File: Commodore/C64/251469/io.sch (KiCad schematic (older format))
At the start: 24 parts, among them CN8 Control Port 2, CN9 Control Port 1, U1 6526, U2 6526, U27 74LS08, U28 4066, U8 7406

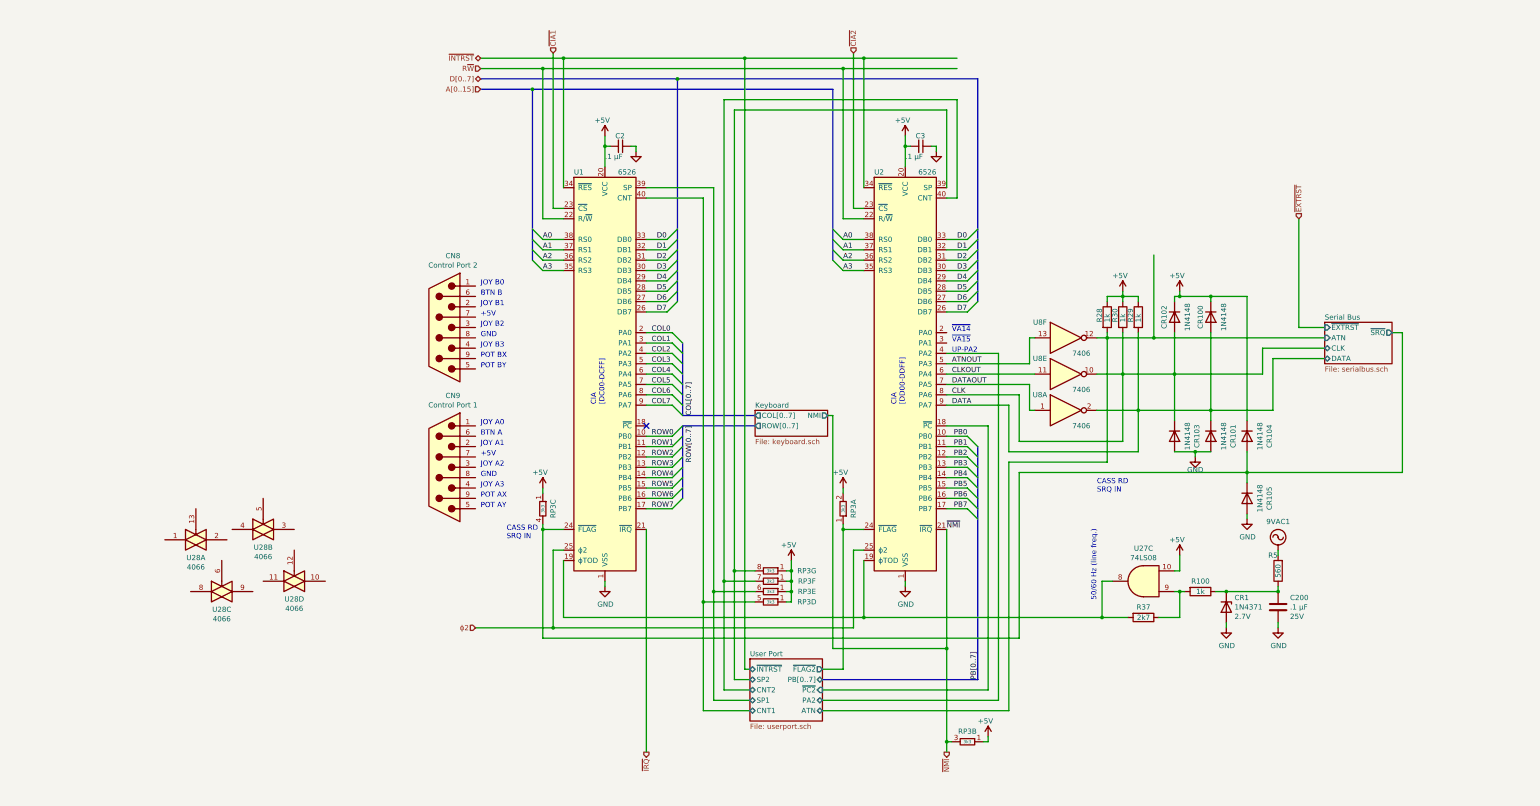
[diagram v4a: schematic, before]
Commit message: Tightened up diode clamp part of IO section
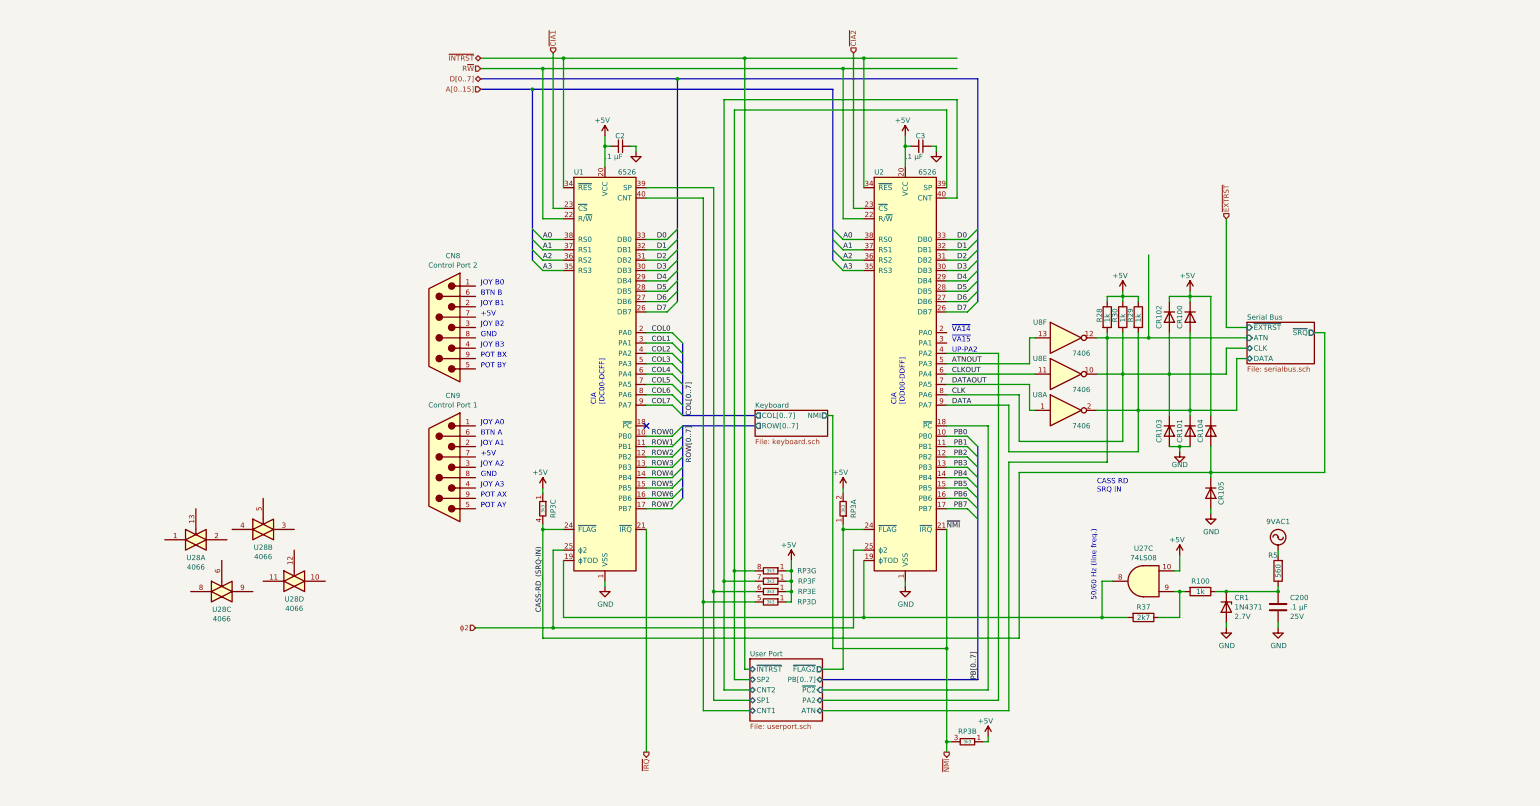
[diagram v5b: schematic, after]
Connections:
- net Serial Bus/~SRQ renamed CASS-RD_(SRQ-IN)
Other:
- moved on the sheet: CR100, CR101, CR102, CR103, CR104, CR105
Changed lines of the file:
@@
 ~NMI
-$Comp
-L Device:D CR101
-U 1 1 5D6E1332
-P 8150 4450
-F 0 "CR101" H 8150 4666 50  0000 C CNN
-F 1 "1N4148" H 8150 4575 50  0000 C CNN
-F 2 "" H 8150 4450 50  0001 C CNN
-F 3 "~" H 8150 4450 50  0001 C CNN
-	1    8150 4450
-	0    1    1    0
-$EndComp
-$Comp
-L Device:D CR103
-U 1 1 5D6E318C
-P 7800 4450
-F 0 "CR103" H 7800 4666 50  0000 C CNN
-F 1 "1N4148" H 7800 4575 50  0000 C CNN
-F 2 "" H 7800 4450 50  0001 C CNN
-F 3 "~" H 7800 4450 50  0001 C CNN
-	1    7800 4450
-	0    1    1    0
-$EndComp
-$Comp
-L Device:D CR104
-U 1 1 5D6E99E9
-P 8500 4450
-F 0 "CR104" H 8500 4666 50  0000 C CNN
-F 1 "1N4148" H 8500 4575 50  0000 C CNN
-F 2 "" H 8500 4450 50  0001 C CNN
-F 3 "~" H 8500 4450 50  0001 C CNN
-	1    8500 4450
-	0    1    1    0
-$EndComp
 $Comp
 L Device:D CR105
 U 1 1 5D6E99EF
-P 8500 5050
-F 0 "CR105" H 8500 5266 50  0000 C CNN
-F 1 "1N4148" H 8500 5175 50  0000 C CNN
-F 2 "" H 8500 5050 50  0001 C CNN
-F 3 "~" H 8500 5050 50  0001 C CNN
-	1    8500 5050
-	0    1    1    0
-$EndComp
-Text Notes 1350 5450 0    50   ~ 0
-CASS RD\nSRQ IN
+P 8150 5000
+F 0 "CR105" H 8150 5100 50  0000 C CNN
+F 1 "1N4148" H 8150 5125 50  0001 C CNN
+F 2 "" H 8150 5000 50  0001 C CNN
+F 3 "~" H 8150 5000 50  0001 C CNN
+	1    8150 5000
+	0    1    1    0
+$EndComp
 Text Notes 5650 3450 0    50   ~ 0
 ~VA14
@@
 Connection ~ 7150 3500
 $Comp
-L Device:R R28
-U 1 1 5DA82DAB
-P 7150 3300
-F 0 "R28" V 7075 3250 50  0000 L CNN
-F 1 "1k" V 7150 3250 50  0000 L CNN
-F 2 "" V 7080 3300 50  0001 C CNN
-F 3 "~" H 7150 3300 50  0001 C CNN
-	1    7150 3300
-	1    0    0    -1
-$EndComp
-$Comp
 L Device:R R30
 U 1 1 5DA836EF
@@
 Connection ~ 7300 3850
 Wire Wire Line
-	7150 3500 7600 3500
+	7150 3500 7550 3500
 Wire Wire Line
 	7050 4200 7450 4200
@@
 	7450 4600 7450 4200
 Wire Wire Line
-	7600 3500 7600 2700
-Wire Wire Line
-	7450 4200 8150 4200
-Wire Wire Line
-	8150 4200 8150 4300
-Connection ~ 7800 3850
-Wire Wire Line
-	7800 3850 7800 4300
-Wire Wire Line
-	7300 3850 7800 3850
-Connection ~ 8150 4200
-Wire Wire Line
-	7800 3850 7800 3450
+	7550 3500 7550 2700
+Wire Wire Line
+	7450 4200 7950 4200
+Connection ~ 7750 3850
+Wire Wire Line
+	7750 3850 7750 4250
+Wire Wire Line
+	7300 3850 7750 3850
+Connection ~ 7950 4200
+Wire Wire Line
+	7750 3850 7750 3450
 $Comp
 L Device:D CR102
 U 1 1 5D6E3186
-P 7800 3300
-F 0 "CR102" H 7800 3200 50  0000 C CNN
-F 1 "1N4148" H 7800 3425 50  0000 C CNN
-F 2 "" H 7800 3300 50  0001 C CNN
-F 3 "~" H 7800 3300 50  0001 C CNN
-	1    7800 3300
-	0    1    1    0
-$EndComp
-Wire Wire Line
-	7800 3150 7800 3100
-Wire Wire Line
-	7850 3100 8150 3100
-Connection ~ 7850 3100
-Wire Wire Line
-	7850 3050 7850 3100
+P 7750 3300
+F 0 "CR102" H 7750 3200 50  0000 C CNN
+F 1 "1N4148" H 7750 3425 50  0001 C CNN
+F 2 "" H 7750 3300 50  0001 C CNN
+F 3 "~" H 7750 3300 50  0001 C CNN
+	1    7750 3300
+	0    1    1    0
+$EndComp
+Wire Wire Line
+	7750 3150 7750 3100
+Wire Wire Line
+	7750 3100 7950 3100
+Wire Wire Line
+	7950 3050 7950 3100
 $Comp
 L power:+5V #PWR?
 U 1 1 5DD390BE
-P 7850 3050
+P 7950 3050
 AR Path="/5DD390BE" Ref="#PWR?"  Part="1"
 AR Path="/5D28EBAC/5DD390BE" Ref="#PWR?"  Part="1"
@@
 AR Path="/5D943305/5DD390BE" Ref="#PWR?"  Part="1"
 AR Path="/5D943305/5D47A471/5DD390BE" Ref="#PWR?"  Part="1"
-F 0 "#PWR?" H 7850 2900 50  0001 C CNN
-F 1 "+5V" H 7750 3200 50  0000 L CNN
-F 2 "" H 7850 3050 50  0001 C CNN
-F 3 "" H 7850 3050 50  0001 C CNN
-	1    7850 3050
-	1    0    0    -1
-$EndComp
-Wire Wire Line
-	8150 3100 8150 3150
-Wire Wire Line
-	7800 3100 7850 3100
-Wire Wire Line
-	8150 4200 8150 3450
+F 0 "#PWR?" H 7950 2900 50  0001 C CNN
+F 1 "+5V" H 7850 3200 50  0000 L CNN
+F 2 "" H 7950 3050 50  0001 C CNN
+F 3 "" H 7950 3050 50  0001 C CNN
+	1    7950 3050
+	1    0    0    -1
+$EndComp
+Wire Wire Line
+	7950 3100 7950 3150
+Wire Wire Line
+	7950 4200 7950 3450
 $Comp
 L Device:D CR100
 U 1 1 5D6E038A
-P 8150 3300
-F 0 "CR100" H 8150 3200 50  0000 C CNN
-F 1 "1N4148" H 8150 3425 50  0000 C CNN
-F 2 "" H 8150 3300 50  0001 C CNN
-F 3 "~" H 8150 3300 50  0001 C CNN
-	1    8150 3300
-	0    1    1    0
-$EndComp
-Connection ~ 7600 3500
+P 7950 3300
+F 0 "CR100" H 7950 3200 50  0000 C CNN
+F 1 "1N4148" H 7950 3425 50  0001 C CNN
+F 2 "" H 7950 3300 50  0001 C CNN
+F 3 "~" H 7950 3300 50  0001 C CNN
+	1    7950 3300
+	0    1    1    0
+$EndComp
+Connection ~ 7550 3500
 $Sheet
-S 9250 3350 650  400
+S 8500 3350 650  400
 U 5DDE0343
 F0 "Serial Bus" 50
 F1 "serialbus.sch" 50
-F2 "~EXTRST" I L 9250 3400 50
-F3 "ATN" I L 9250 3500 50
-F4 "CLK" B L 9250 3600 50
-F5 "DATA" B L 9250 3700 50
-F6 "~SRQ" O R 9900 3450 50
+F2 "~EXTRST" I L 8500 3400 50
+F3 "ATN" I L 8500 3500 50
+F4 "CLK" B L 8500 3600 50
+F5 "DATA" B L 8500 3700 50
+F6 "~SRQ" O R 9150 3450 50
 $EndSheet
 Connection ~ 4600 5350
@@
 Connection ~ 1700 5350
 Wire Wire Line
-	6300 4800 8500 4800
-Wire Wire Line
-	8150 4200 8750 4200
-Wire Wire Line
-	7800 3850 8650 3850
-Wire Wire Line
-	8500 4300 8500 3100
-Wire Wire Line
-	8500 3100 8150 3100
-Connection ~ 8150 3100
-Wire Wire Line
-	8500 4800 8500 4600
-Connection ~ 8500 4800
-Wire Wire Line
-	8500 4800 8500 4900
-Wire Wire Line
-	8150 4600 8000 4600
-$Comp
-L power:GND #PWR?
-U 1 1 5DFF36EE
-P 8000 4650
-F 0 "#PWR?" H 8000 4400 50  0001 C CNN
-F 1 "GND" H 8000 4525 50  0000 C CNN
-F 2 "" H 8000 4650 50  0001 C CNN
-F 3 "" H 8000 4650 50  0001 C CNN
-	1    8000 4650
-	1    0    0    -1
-$EndComp
-Wire Wire Line
-	8000 4650 8000 4600
-Connection ~ 8000 4600
-Wire Wire Line
-	8000 4600 7800 4600
+	6300 4800 8150 4800
+Wire Wire Line
+	7950 4200 8400 4200
+Wire Wire Line
+	7750 3850 8300 3850
+Wire Wire Line
+	8150 3100 7950 3100
+Connection ~ 7950 3100
+Connection ~ 8150 4800
+Wire Wire Line
+	8150 4800 8150 4850
 $Comp
 L power:GND #PWR?
 U 1 1 5E000C0D
-P 8500 5250
-F 0 "#PWR?" H 8500 5000 50  0001 C CNN
-F 1 "GND" H 8505 5077 50  0000 C CNN
-F 2 "" H 8500 5250 50  0001 C CNN
-F 3 "" H 8500 5250 50  0001 C CNN
-	1    8500 5250
-	1    0    0    -1
-$EndComp
-Wire Wire Line
-	8500 5250 8500 5200
-Wire Wire Line
-	10000 4800 10000 3450
-Wire Wire Line
-	8500 4800 10000 4800
-Wire Wire Line
-	7600 3500 9250 3500
-Wire Wire Line
-	9250 3400 9000 3400
-Wire Wire Line
-	9000 3400 9000 2350
-Text HLabel 9000 2350 1    50   Input ~ 0
+P 8150 5200
+F 0 "#PWR?" H 8150 4950 50  0001 C CNN
+F 1 "GND" H 8155 5027 50  0000 C CNN
+F 2 "" H 8150 5200 50  0001 C CNN
+F 3 "" H 8150 5200 50  0001 C CNN
+	1    8150 5200
+	1    0    0    -1
+$EndComp
+Wire Wire Line
+	8150 5200 8150 5150
+Wire Wire Line
+	9250 4800 9250 3450
+Wire Wire Line
+	8150 4800 9250 4800
+Wire Wire Line
+	7550 3500 8500 3500
+Wire Wire Line
+	8500 3400 8300 3400
+Wire Wire Line
+	8300 3400 8300 2350
+Text HLabel 8300 2350 1    50   Input ~ 0
 ~EXTRST
 Wire Wire Line
-	8650 3600 9250 3600
-Wire Wire Line
-	8650 3600 8650 3850
-Wire Wire Line
-	8750 3700 9250 3700
-Wire Wire Line
-	8750 3700 8750 4200
-Wire Wire Line
-	10000 3450 9900 3450
+	8300 3600 8500 3600
+Wire Wire Line
+	8300 3600 8300 3850
+Wire Wire Line
+	8400 3700 8500 3700
+Wire Wire Line
+	8400 3700 8400 4200
+Wire Wire Line
+	9250 3450 9150 3450
 Wire Wire Line
 	4600 4950 4600 5000
@@
 F 3 "http://www.vishay.com/docs/31509/csc.pdf" H 3900 6050 50  0001 C CNN
 	4    3900 6050
+	0    1    1    0
+$EndComp
+Text Label 5600 5350 0    50   ~ 0
+~NMI
+Text Label 5650 3750 0    50   ~ 0
+ATNOUT
+Text Label 5650 3850 0    50   ~ 0
+CLKOUT
+Text Label 5650 3950 0    50   ~ 0
+DATAOUT
+Text Label 5650 4050 0    50   ~ 0
+CLK
+Text Label 5650 4150 0    50   ~ 0
+DATA
+$Comp
+L Device:R R28
+U 1 1 5DA82DAB
+P 7150 3300
+F 0 "R28" V 7075 3250 50  0000 L CNN
+F 1 "1k" V 7150 3250 50  0000 L CNN
+F 2 "" V 7080 3300 50  0001 C CNN
+F 3 "~" H 7150 3300 50  0001 C CNN
+	1    7150 3300
+	1    0    0    -1
+$EndComp
+$Comp
+L Device:D CR103
+U 1 1 5D6E318C
+P 7750 4400
+F 0 "CR103" H 7750 4300 50  0000 C CNN
+F 1 "1N4148" H 7750 4500 50  0001 C CNN
+F 2 "" H 7750 4400 50  0001 C CNN
+F 3 "~" H 7750 4400 50  0001 C CNN
+	1    7750 4400
+	0    1    1    0
+$EndComp
+Wire Wire Line
+	7750 4550 7850 4550
+$Comp
+L power:GND #PWR?
+U 1 1 5DFF36EE
+P 7850 4600
+F 0 "#PWR?" H 7850 4350 50  0001 C CNN
+F 1 "GND" H 7850 4475 50  0000 C CNN
+F 2 "" H 7850 4600 50  0001 C CNN
+F 3 "" H 7850 4600 50  0001 C CNN
+	1    7850 4600
+	1    0    0    -1
+$EndComp
+Wire Wire Line
+	7850 4600 7850 4550
+Connection ~ 7850 4550
+Wire Wire Line
+	7850 4550 7950 4550
+Wire Wire Line
+	7950 4200 7950 4250
+$Comp
+L Device:D CR101
+U 1 1 5D6E1332
+P 7950 4400
+F 0 "CR101" H 7950 4300 50  0000 C CNN
+F 1 "1N4148" H 7950 4500 50  0001 C CNN
+F 2 "" H 7950 4400 50  0001 C CNN
+F 3 "~" H 7950 4400 50  0001 C CNN
+	1    7950 4400
+	0    1    1    0
+$EndComp
+Wire Wire Line
+	8150 4800 8150 4550
+Wire Wire Line
+	8150 4250 8150 3100
+$Comp
+L Device:D CR104
+U 1 1 5D6E99E9
+P 8150 4400
+F 0 "CR104" H 8150 4300 50  0000 C CNN
+F 1 "1N4148" H 8150 4500 50  0001 C CNN
+F 2 "" H 8150 4400 50  0001 C CNN
+F 3 "~" H 8150 4400 50  0001 C CNN
+	1    8150 4400
 	0    1    1    0
 $EndComp
@@
 Wire Bus Line
 	3000 1000 3000 3150
-Text Label 5600 5350 0    50   ~ 0
-~NMI
-Text Label 5650 3750 0    50   ~ 0
-ATNOUT
-Text Label 5650 3850 0    50   ~ 0
-CLKOUT
-Text Label 5650 3950 0    50   ~ 0
-DATAOUT
-Text Label 5650 4050 0    50   ~ 0
-CLK
-Text Label 5650 4150 0    50   ~ 0
-DATA
+Text Label 1700 6150 1    50   ~ 0
+CASS-RD_(SRQ-IN)
 $EndSCHEMATC

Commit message: WIP
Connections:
- net TOD: now reaches R37.2, U1.19 (ϕTOD), U2.19 (ϕTOD), U27.8
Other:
- note removed: "CASS RD\nSRQ IN"
- moved on the sheet: C200, CR1, R100, R37, R5, U27C
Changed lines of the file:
@@
 L Device:R R37
 U 1 1 5D3AB7B9
-P 7500 6200
-F 0 "R37" V 7400 6200 50  0000 C CNN
-F 1 "2k7" V 7500 6200 50  0000 C CNN
-F 2 "" V 7430 6200 50  0001 C CNN
-F 3 "~" H 7500 6200 50  0001 C CNN
-	1    7500 6200
+P 9550 6200
+F 0 "R37" V 9450 6200 50  0000 C CNN
+F 1 "2k7" V 9550 6200 50  0000 C CNN
+F 2 "" V 9480 6200 50  0001 C CNN
+F 3 "~" H 9550 6200 50  0001 C CNN
+	1    9550 6200
 	0    1    1    0
 $EndComp
@@
 L Device:R R100
 U 1 1 5D3AC837
-P 8050 5950
-F 0 "R100" V 7950 5950 50  0000 C CNN
-F 1 "1k" V 8050 5950 50  0000 C CNN
-F 2 "" V 7980 5950 50  0001 C CNN
-F 3 "~" H 8050 5950 50  0001 C CNN
-	1    8050 5950
+P 10100 5950
+F 0 "R100" V 10000 5950 50  0000 C CNN
+F 1 "1k" V 10100 5950 50  0000 C CNN
+F 2 "" V 10030 5950 50  0001 C CNN
+F 3 "~" H 10100 5950 50  0001 C CNN
+	1    10100 5950
 	0    1    1    0
 $EndComp
@@
 L Device:D_Zener CR1
 U 1 1 5D3AF3BF
-P 8300 6100
-F 0 "CR1" V 8209 6179 50  0000 L CNN
-F 1 "1N4371" V 8300 6179 50  0000 L CNN
-F 2 "" H 8300 6100 50  0001 C CNN
-F 3 "~" H 8300 6100 50  0001 C CNN
-F 4 "2.7V" V 8391 6179 50  0000 L CNN "Zener Voltage"
-	1    8300 6100
+P 10350 6100
+F 0 "CR1" V 10259 6179 50  0000 L CNN
+F 1 "1N4371" V 10350 6179 50  0000 L CNN
+F 2 "" H 10350 6100 50  0001 C CNN
+F 3 "~" H 10350 6100 50  0001 C CNN
+F 4 "2.7V" V 10441 6179 50  0000 L CNN "Zener Voltage"
+	1    10350 6100
 	0    1    1    0
 $EndComp
@@
 L Device:C C200
 U 1 1 5D3B049D
-P 8800 6100
-F 0 "C200" H 8915 6191 50  0000 L CNN
-F 1 ".1 μF" H 8915 6100 50  0000 L CNN
-F 2 "" H 8838 5950 50  0001 C CNN
-F 3 "~" H 8800 6100 50  0001 C CNN
-F 4 "25V" H 8915 6009 50  0000 L CNN "Voltage Rating"
-	1    8800 6100
+P 10850 6100
+F 0 "C200" H 10965 6191 50  0000 L CNN
+F 1 ".1 μF" H 10965 6100 50  0000 L CNN
+F 2 "" H 10888 5950 50  0001 C CNN
+F 3 "~" H 10850 6100 50  0001 C CNN
+F 4 "25V" H 10965 6009 50  0000 L CNN "Voltage Rating"
+	1    10850 6100
 	1    0    0    -1
 $EndComp
@@
 L power_more:9VAC1 #PWR?
 U 1 1 5D3B15DC
-P 8800 5550
-F 0 "#PWR?" H 8800 5450 50  0001 C CNN
-F 1 "9VAC1" H 8800 5825 50  0000 C CNN
-F 2 "" H 8800 5550 50  0001 C CNN
-F 3 "" H 8800 5550 50  0001 C CNN
-	1    8800 5550
-	1    0    0    -1
-$EndComp
-Wire Wire Line
-	8800 5550 8800 5600
-Wire Wire Line
-	8800 5900 8800 5950
+P 10850 5550
+F 0 "#PWR?" H 10850 5450 50  0001 C CNN
+F 1 "9VAC1" H 10850 5825 50  0000 C CNN
+F 2 "" H 10850 5550 50  0001 C CNN
+F 3 "" H 10850 5550 50  0001 C CNN
+	1    10850 5550
+	1    0    0    -1
+$EndComp
+Wire Wire Line
+	10850 5550 10850 5600
+Wire Wire Line
+	10850 5900 10850 5950
 $Comp
 L power:GND #PWR?
 U 1 1 5D3B771F
-P 8800 6300
-F 0 "#PWR?" H 8800 6050 50  0001 C CNN
-F 1 "GND" H 8805 6127 50  0000 C CNN
-F 2 "" H 8800 6300 50  0001 C CNN
-F 3 "" H 8800 6300 50  0001 C CNN
-	1    8800 6300
-	1    0    0    -1
-$EndComp
-Wire Wire Line
-	8800 6250 8800 6300
+P 10850 6300
+F 0 "#PWR?" H 10850 6050 50  0001 C CNN
+F 1 "GND" H 10855 6127 50  0000 C CNN
+F 2 "" H 10850 6300 50  0001 C CNN
+F 3 "" H 10850 6300 50  0001 C CNN
+	1    10850 6300
+	1    0    0    -1
+$EndComp
+Wire Wire Line
+	10850 6250 10850 6300
 $Comp
 L power:GND #PWR?
 U 1 1 5D3B8BE9
-P 8300 6300
-F 0 "#PWR?" H 8300 6050 50  0001 C CNN
-F 1 "GND" H 8305 6127 50  0000 C CNN
-F 2 "" H 8300 6300 50  0001 C CNN
-F 3 "" H 8300 6300 50  0001 C CNN
-	1    8300 6300
-	1    0    0    -1
-$EndComp
-Wire Wire Line
-	8300 6250 8300 6300
-Wire Wire Line
-	8300 5950 8800 5950
-Connection ~ 8800 5950
+P 10350 6300
+F 0 "#PWR?" H 10350 6050 50  0001 C CNN
+F 1 "GND" H 10355 6127 50  0000 C CNN
+F 2 "" H 10350 6300 50  0001 C CNN
+F 3 "" H 10350 6300 50  0001 C CNN
+	1    10350 6300
+	1    0    0    -1
+$EndComp
+Wire Wire Line
+	10350 6250 10350 6300
+Wire Wire Line
+	10350 5950 10850 5950
+Connection ~ 10850 5950
 $Comp
 L Device:R R5
 U 1 1 5D3AD8AF
-P 8800 5750
-F 0 "R5" H 8850 5600 50  0000 C CNN
-F 1 "560" V 8800 5750 50  0000 C CNN
-F 2 "" V 8730 5750 50  0001 C CNN
-F 3 "~" H 8800 5750 50  0001 C CNN
-	1    8800 5750
+P 10850 5750
+F 0 "R5" H 10900 5600 50  0000 C CNN
+F 1 "560" V 10850 5750 50  0000 C CNN
+F 2 "" V 10780 5750 50  0001 C CNN
+F 3 "~" H 10850 5750 50  0001 C CNN
+	1    10850 5750
 	-1   0    0    1
 $EndComp
@@
 L power:+5V #PWR?
 U 1 1 5D3C4989
-P 7850 5600
+P 9900 5600
 AR Path="/5D3C4989" Ref="#PWR?"  Part="1"
 AR Path="/5D28EBAC/5D3C4989" Ref="#PWR?"  Part="1"
 AR Path="/5D4AE438/5D3C4989" Ref="#PWR?"  Part="1"
 AR Path="/5D943305/5D3C4989" Ref="#PWR?"  Part="1"
-F 0 "#PWR?" H 7850 5450 50  0001 C CNN
-F 1 "+5V" H 7750 5750 50  0000 L CNN
-F 2 "" H 7850 5600 50  0001 C CNN
-F 3 "" H 7850 5600 50  0001 C CNN
-	1    7850 5600
-	1    0    0    -1
-$EndComp
-Wire Wire Line
-	7850 5750 7850 5600
-Wire Wire Line
-	7800 5750 7850 5750
+F 0 "#PWR?" H 9900 5450 50  0001 C CNN
+F 1 "+5V" H 9800 5750 50  0000 L CNN
+F 2 "" H 9900 5600 50  0001 C CNN
+F 3 "" H 9900 5600 50  0001 C CNN
+	1    9900 5600
+	1    0    0    -1
+$EndComp
+Wire Wire Line
+	9900 5750 9900 5600
+Wire Wire Line
+	9850 5750 9900 5750
 $Comp
 L 74xx:74LS08 U27
 U 3 1 5D393DE7
-P 7500 5850
-F 0 "U27" H 7500 5533 50  0000 C CNN
-F 1 "74LS08" H 7500 5624 50  0000 C CNN
-F 2 "" H 7500 5850 50  0001 C CNN
-F 3 "http://www.ti.com/lit/gpn/sn74LS08" H 7500 5850 50  0001 C CNN
-	3    7500 5850
+P 9550 5850
+F 0 "U27" H 9550 5533 50  0000 C CNN
+F 1 "74LS08" H 9550 5624 50  0000 C CNN
+F 2 "" H 9550 5850 50  0001 C CNN
+F 3 "http://www.ti.com/lit/gpn/sn74LS08" H 9550 5850 50  0001 C CNN
+	3    9550 5850
 	-1   0    0    1
 $EndComp
-Connection ~ 8300 5950
-Wire Wire Line
-	8200 5950 8300 5950
-Wire Wire Line
-	7350 6200 7100 6200
-Wire Wire Line
-	7200 5850 7100 5850
-Wire Wire Line
-	7800 5950 7850 5950
-Wire Wire Line
-	7650 6200 7850 6200
-Wire Wire Line
-	7850 6200 7850 5950
-Connection ~ 7850 5950
-Wire Wire Line
-	7850 5950 7900 5950
-Text Notes 7050 5350 3    50   ~ 0
+Connection ~ 10350 5950
+Wire Wire Line
+	10250 5950 10350 5950
+Wire Wire Line
+	9400 6200 9150 6200
+Wire Wire Line
+	9250 5850 9150 5850
+Wire Wire Line
+	9850 5950 9900 5950
+Wire Wire Line
+	9700 6200 9900 6200
+Wire Wire Line
+	9900 6200 9900 5950
+Connection ~ 9900 5950
+Wire Wire Line
+	9900 5950 9950 5950
+Text Notes 8100 6200 0    50   ~ 0
 50/60 Hz (line freq.)
 Wire Wire Line
-	4800 6200 7100 6200
+	4800 6200 9150 6200
 Connection ~ 4800 6200
 Wire Wire Line
@@
 	4500 6500 5600 6500
 Wire Wire Line
-	7100 5850 7100 6200
-Connection ~ 7100 6200
+	9150 5850 9150 6200
+Connection ~ 9150 6200
 $Comp
 L 74xx_more:7406 U8
@@
 Wire Wire Line
 	6300 6400 6300 4800
-Text Notes 7050 5000 0    50   ~ 0
-CASS RD\nSRQ IN
 $Comp
 L power:+5V #PWR?
@@
 	0    1    1    0
 $EndComp
-Wire Bus Line
-	4500 1100 4500 2750
-Wire Bus Line
-	1600 1100 1600 2750
-Wire Bus Line
-	3050 4350 3050 5050
-Wire Bus Line
-	3050 3550 3050 4250
-Wire Bus Line
-	5900 4550 5900 6800
-Wire Bus Line
-	5900 1000 5900 3150
-Wire Bus Line
-	3000 1000 3000 3150
 Text Label 1700 6150 1    50   ~ 0
 CASS-RD_(SRQ-IN)
+Wire Bus Line
+	4500 1100 4500 2750
+Wire Bus Line
+	1600 1100 1600 2750
+Wire Bus Line
+	3050 4350 3050 5050
+Wire Bus Line
+	3050 3550 3050 4250
+Wire Bus Line
+	5900 4550 5900 6800
+Wire Bus Line
+	5900 1000 5900 3150
+Wire Bus Line
+	3000 1000 3000 3150
+Text Label 9000 6200 0    50   ~ 0
+TOD
 $EndSCHEMATC
